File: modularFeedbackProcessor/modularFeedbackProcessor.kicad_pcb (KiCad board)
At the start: 2 copper layers, 191.5 x 124 mm, 203 parts, among them J1 Input, J10 Output, J2 Feedback, J4 Eurorack_Power_16pin_Unshroud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, J5 DryWet, J6 Rate, J7 EffectsRouteIn, J8 EffectsRouteOut, J9 EffectsDryWet, Q1 Q_PMOS_GDS, Q10 Q_PMOS_GDS, Q11 Q_NMOS_GDS, Q12 Q_PMOS_GDS, Q13 Q_PMOS_GDS, Q14 Q_NMOS_GDS, Q15 Q_PMOS_GDS, Q16 Q_NMOS_GDS, Q17 Q_PMOS_GDS, Q18 Q_NMOS_GDS, Q19 Q_PMOS_GDS, Q2 Q_NMOS_GDS, Q3 Q_PMOS_GDS, Q4 Q_PMOS_GDS, Q5 Q_NMOS_GDS, Q6 Q_PMOS_GDS, Q7 Q_NMOS_GDS, Q8 Q_PMOS_GDS, Q9 Q_NMOS_GDS, SW1 EffectsRouting, U1 TL074, U10 LM13700, U2 TL074, U3 LM13700, U4 V3205, U5 CD4046, U6 LF398_DIP8, U7 TL074, U8 LM13700, U9 TL074

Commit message: finished final tweaks before JLC
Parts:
- moved R43 14.0 mm to (106.5, 40.5), turned to 180 degrees
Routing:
- net Net-(R42-Pad2): track 129.0 -> 113.2 mm
- net Net-(J10-T): track 7.03 -> 6.10 mm
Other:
- board text added: "CV Level"
- board text added: "Designed by Jet Trommer"
- board text added: "Dry/Wet"
- board text added: "Effect Dry/Wet"
- board text added: "Effect In"
- board text added: "Effect Out"
- board text added: "Feedback"
- board text added: "Feedback Processor V1"
- board text added: "Gain"
- board text added: "Input"
- board text added: "Offset"
- board text added: "Output"
- board text added: "Rate"

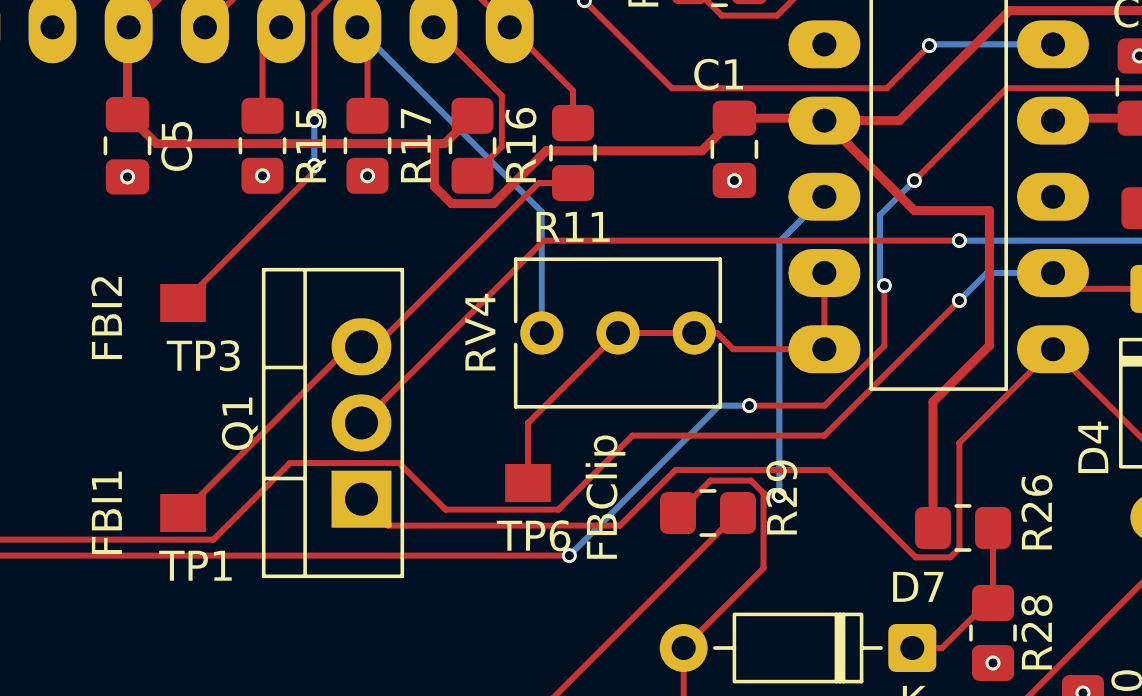
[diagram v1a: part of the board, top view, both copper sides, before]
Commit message: fixed Q1 on PCB.
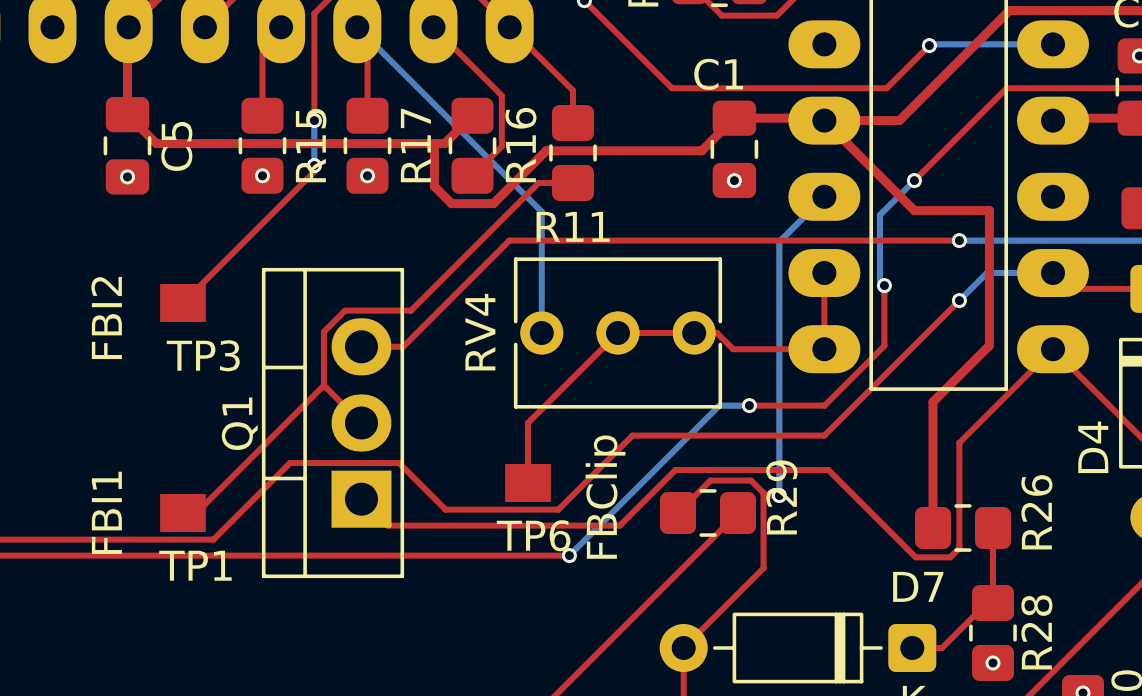
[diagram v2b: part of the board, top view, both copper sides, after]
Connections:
- R10 pad 1: Net-(Q1-D) -> Net-(Q1-S)
- R11 pad 2: Net-(Q1-S) -> Net-(Q1-D)
- R9 pad 2: Net-(Q1-D) -> Net-(Q1-S)
- TP1 pad 1: Net-(Q1-S) -> Net-(Q1-D)
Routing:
- net Net-(Q1-S): track 17.6 -> 34.7 mm, vias 0 -> 3
- net Net-(Q1-D): track 34.9 -> 20.4 mm, vias 3 -> 0
